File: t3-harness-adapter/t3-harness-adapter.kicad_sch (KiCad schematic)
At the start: 1 part, among them J1 Conn_01x14_Pin

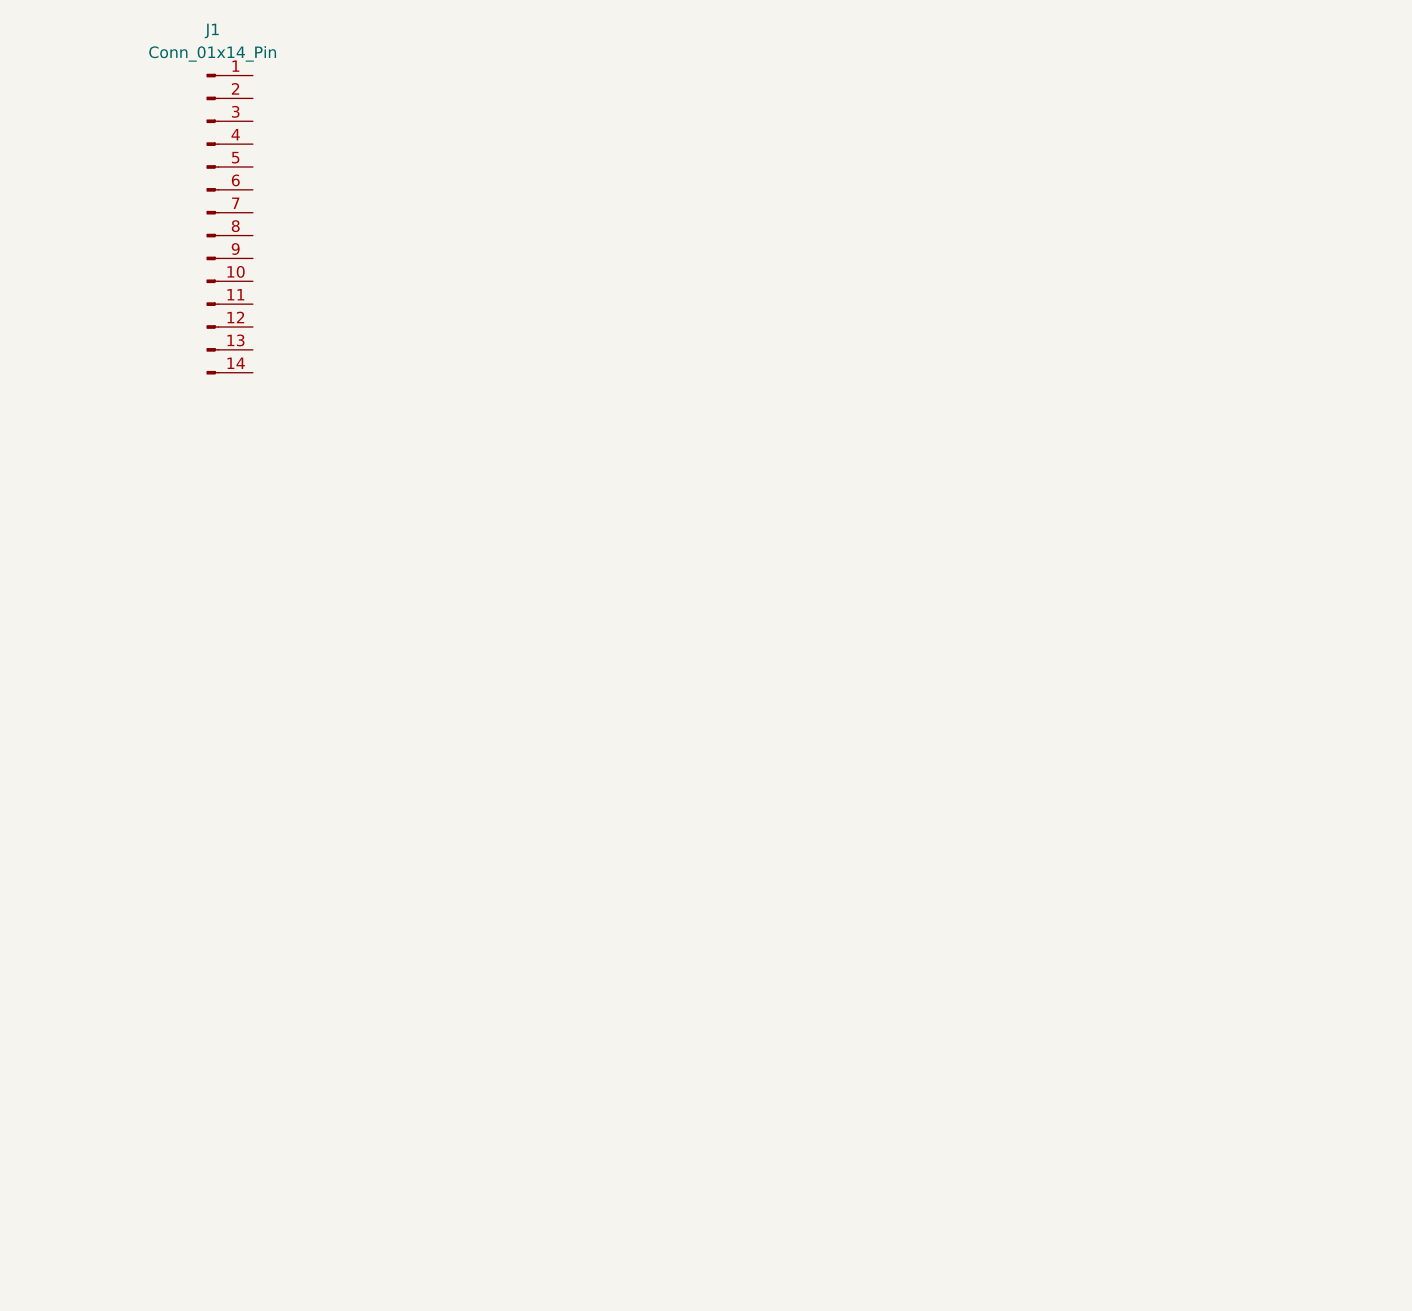
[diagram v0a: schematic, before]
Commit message: [schematic] added all used connectors
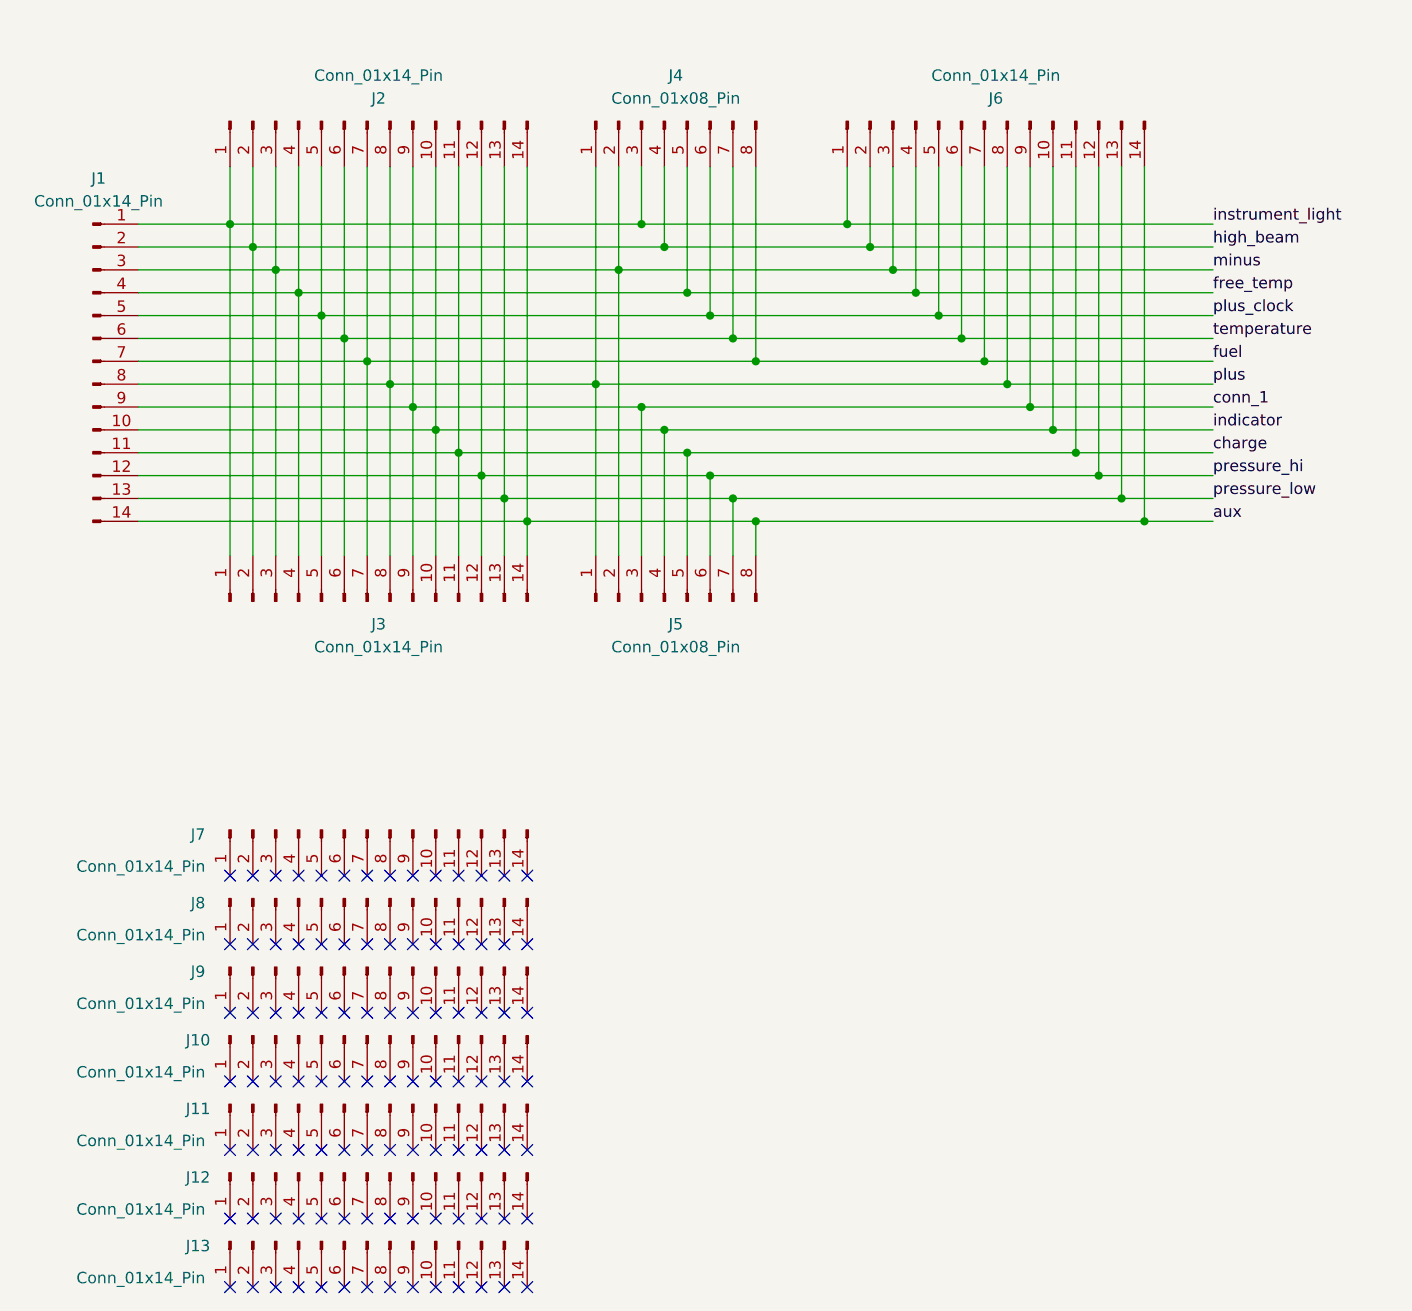
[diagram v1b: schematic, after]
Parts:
- added J10, J11, J12, J13, J2, J3, J6, J7, J8, J9: Conn_01x14_Pin, Connector_PinHeader_2.54mm:PinHeader_1x14_P2.54mm_Vertical, symbol Connector:Conn_01x14_Pin
- added J4, J5: Conn_01x08_Pin, Connector_PinHeader_2.54mm:PinHeader_2x04_P2.54mm_Vertical, symbol Connector:Conn_01x08_Pin
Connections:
- net instrument_light: now reaches J1.1 (Pin_1)
- net instrument_light: now also J2.1 (Pin_1), J3.1 (Pin_1), J4.3 (Pin_3), J6.1 (Pin_1)
- net indicator: now reaches J1.10 (Pin_10)
- net indicator: now also J2.10 (Pin_10), J3.10 (Pin_10), J5.4 (Pin_4), J6.10 (Pin_10)
- net charge: now reaches J1.11 (Pin_11)
- net charge: now also J2.11 (Pin_11), J3.11 (Pin_11), J5.5 (Pin_5), J6.11 (Pin_11)
- net pressure_hi: now reaches J1.12 (Pin_12)
- net pressure_hi: now also J2.12 (Pin_12), J3.12 (Pin_12), J5.6 (Pin_6), J6.12 (Pin_12)
- net pressure_low: now reaches J1.13 (Pin_13)
- net pressure_low: now also J2.13 (Pin_13), J3.13 (Pin_13), J5.7 (Pin_7), J6.13 (Pin_13)
- net aux: now reaches J1.14 (Pin_14)
- net aux: now also J2.14 (Pin_14), J3.14 (Pin_14), J5.8 (Pin_8), J6.14 (Pin_14)
- net high_beam: now reaches J1.2 (Pin_2)
- net high_beam: now also J2.2 (Pin_2), J3.2 (Pin_2), J4.4 (Pin_4), J6.2 (Pin_2)
- net minus: now reaches J1.3 (Pin_3)
- net minus: now also J2.3 (Pin_3), J3.3 (Pin_3), J4.2 (Pin_2), J5.2 (Pin_2), J6.3 (Pin_3)
- net free_temp: now reaches J1.4 (Pin_4)
- net free_temp: now also J2.4 (Pin_4), J3.4 (Pin_4), J4.5 (Pin_5), J6.4 (Pin_4)
- net plus_clock: now reaches J1.5 (Pin_5)
- net plus_clock: now also J2.5 (Pin_5), J3.5 (Pin_5), J4.6 (Pin_6), J6.5 (Pin_5)
- net temperature: now reaches J1.6 (Pin_6)
- net temperature: now also J2.6 (Pin_6), J3.6 (Pin_6), J4.7 (Pin_7), J6.6 (Pin_6)
- net fuel: now reaches J1.7 (Pin_7)
- net fuel: now also J2.7 (Pin_7), J3.7 (Pin_7), J4.8 (Pin_8), J6.7 (Pin_7)
- net plus: now reaches J1.8 (Pin_8)
- net plus: now also J2.8 (Pin_8), J3.8 (Pin_8), J4.1 (Pin_1), J5.1 (Pin_1), J6.8 (Pin_8)
- net conn_1: now reaches J1.9 (Pin_9)
- net conn_1: now also J2.9 (Pin_9), J3.9 (Pin_9), J5.3 (Pin_3), J6.9 (Pin_9)
- no-connect marks 0 -> 98
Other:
- moved on the sheet: J1
